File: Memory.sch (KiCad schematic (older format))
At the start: 16 parts, among them U10 74LS05, U11 74HCT00, U12 74LS32, U2 AS6C4008-55PCN, U3 AS6C4008-55PCN, U4 AS6C4008-55PCN, U5 AS6C4008-55PCN, U6 74HCT00, U7 74LS32, U8 74LS32, U9 74LS05

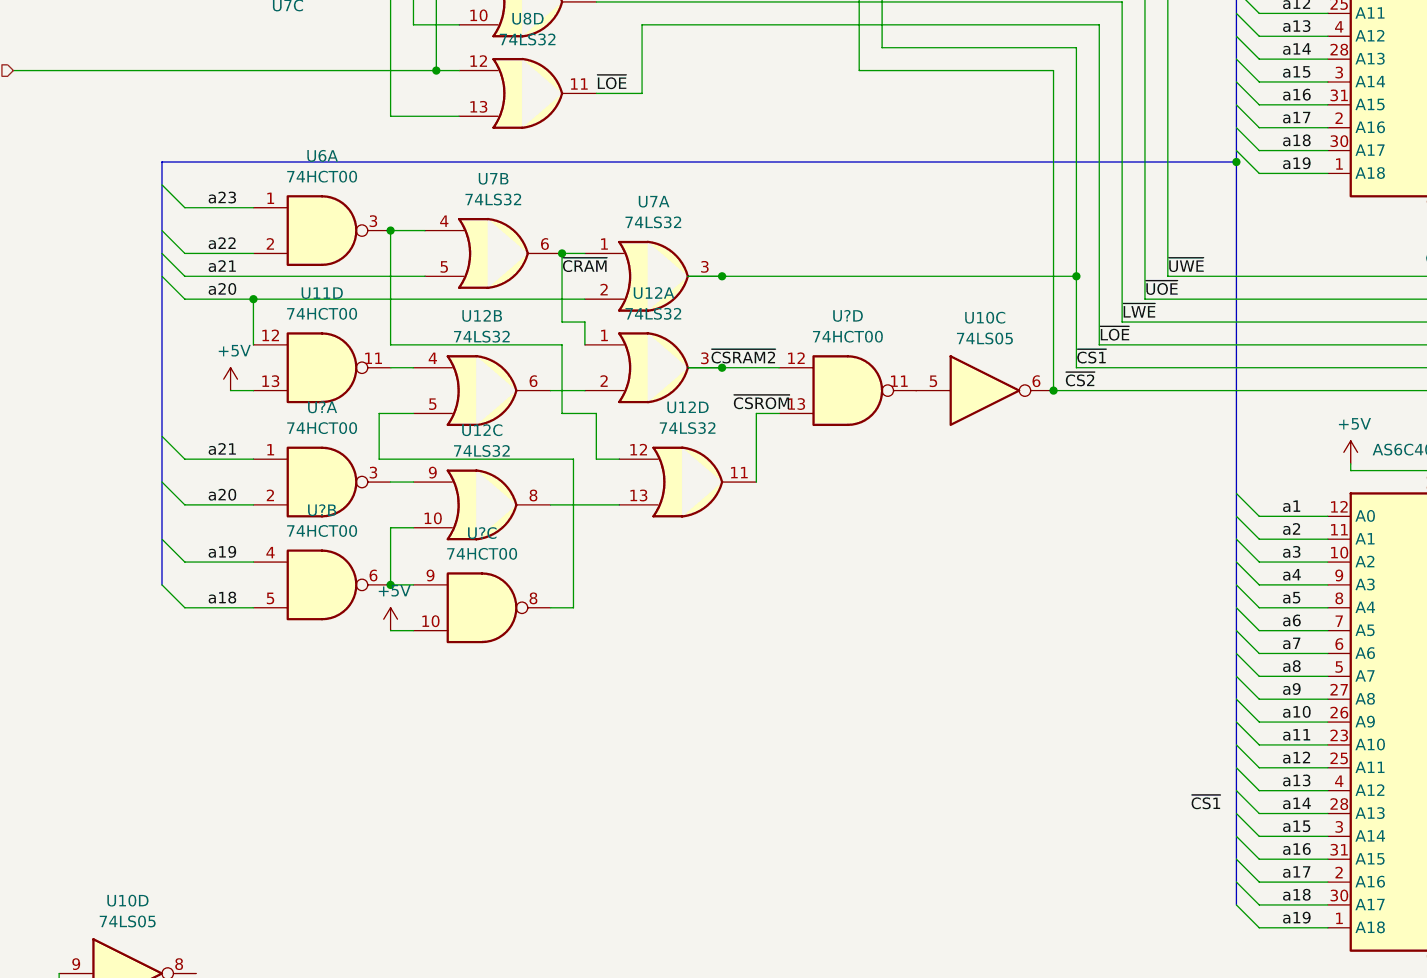
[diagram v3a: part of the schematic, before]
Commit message: jumper for rom size
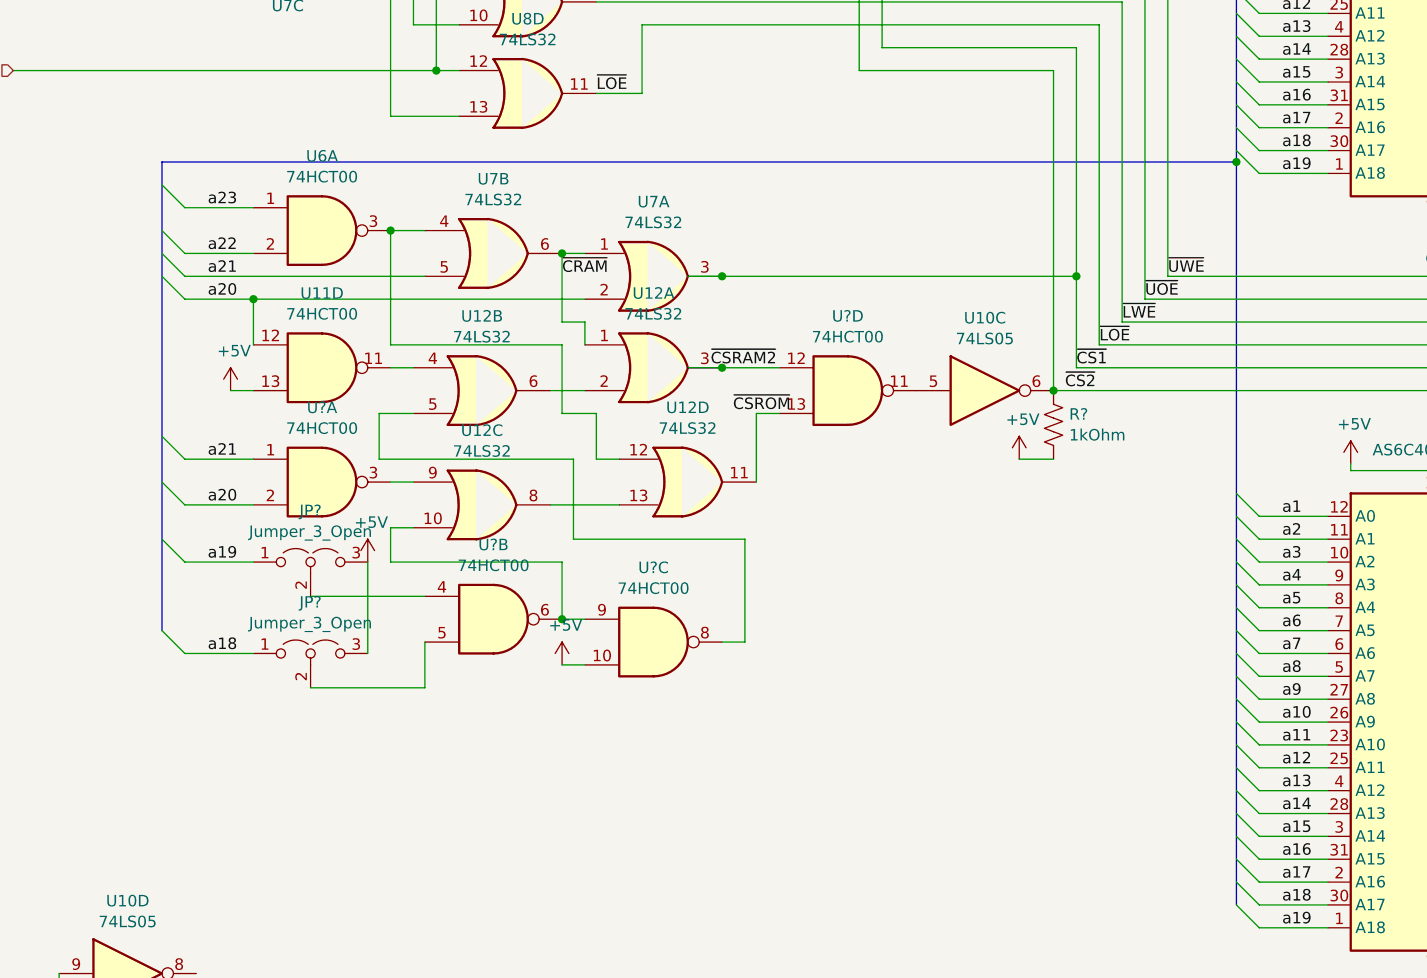
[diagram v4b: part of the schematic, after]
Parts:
- added JP? (x2): Jumper_3_Open, symbol jumper:Jumper_3_Open
- added R?: 1kOhm, symbol device:R_US
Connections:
- net +5V: now also JP?.3 (B), JP?.3 (B), R?.2
- net a18: now also JP?.1 (A); no longer U?.5
- net a19: now also JP?.1 (A); no longer U?.4
- net ~CS2: now also R?.1
- new net: JP?.2 (C), U?.5
- new net: JP?.2 (C), U?.4
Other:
- moved on the sheet: U?B, U?C

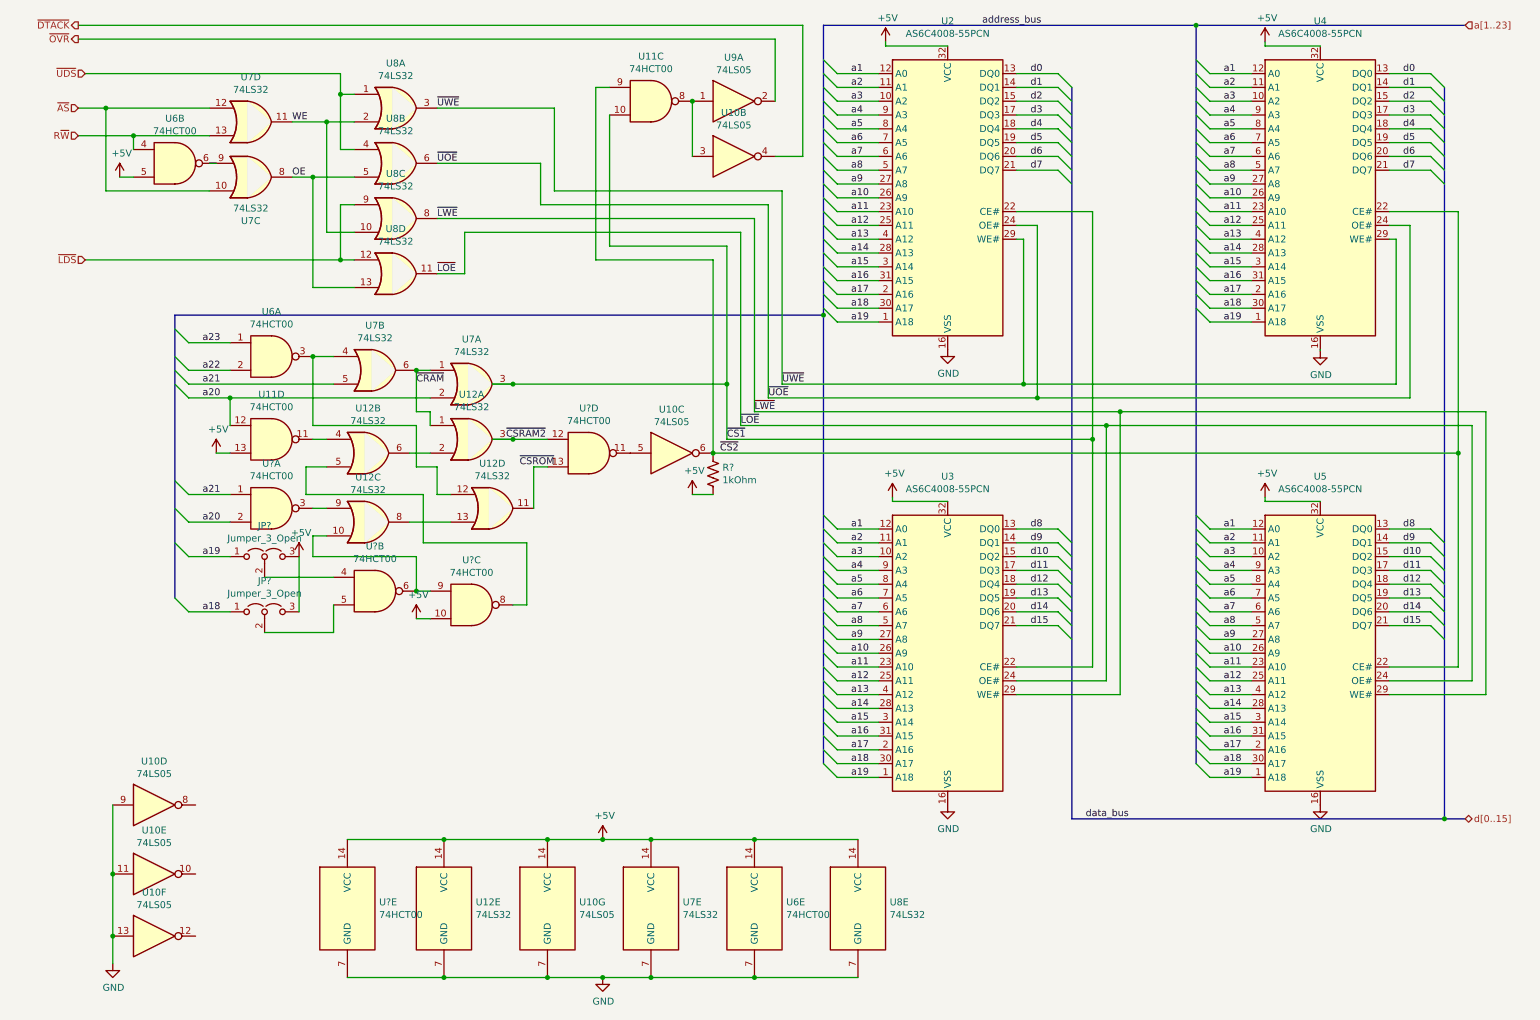
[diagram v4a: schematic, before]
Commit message: add battery
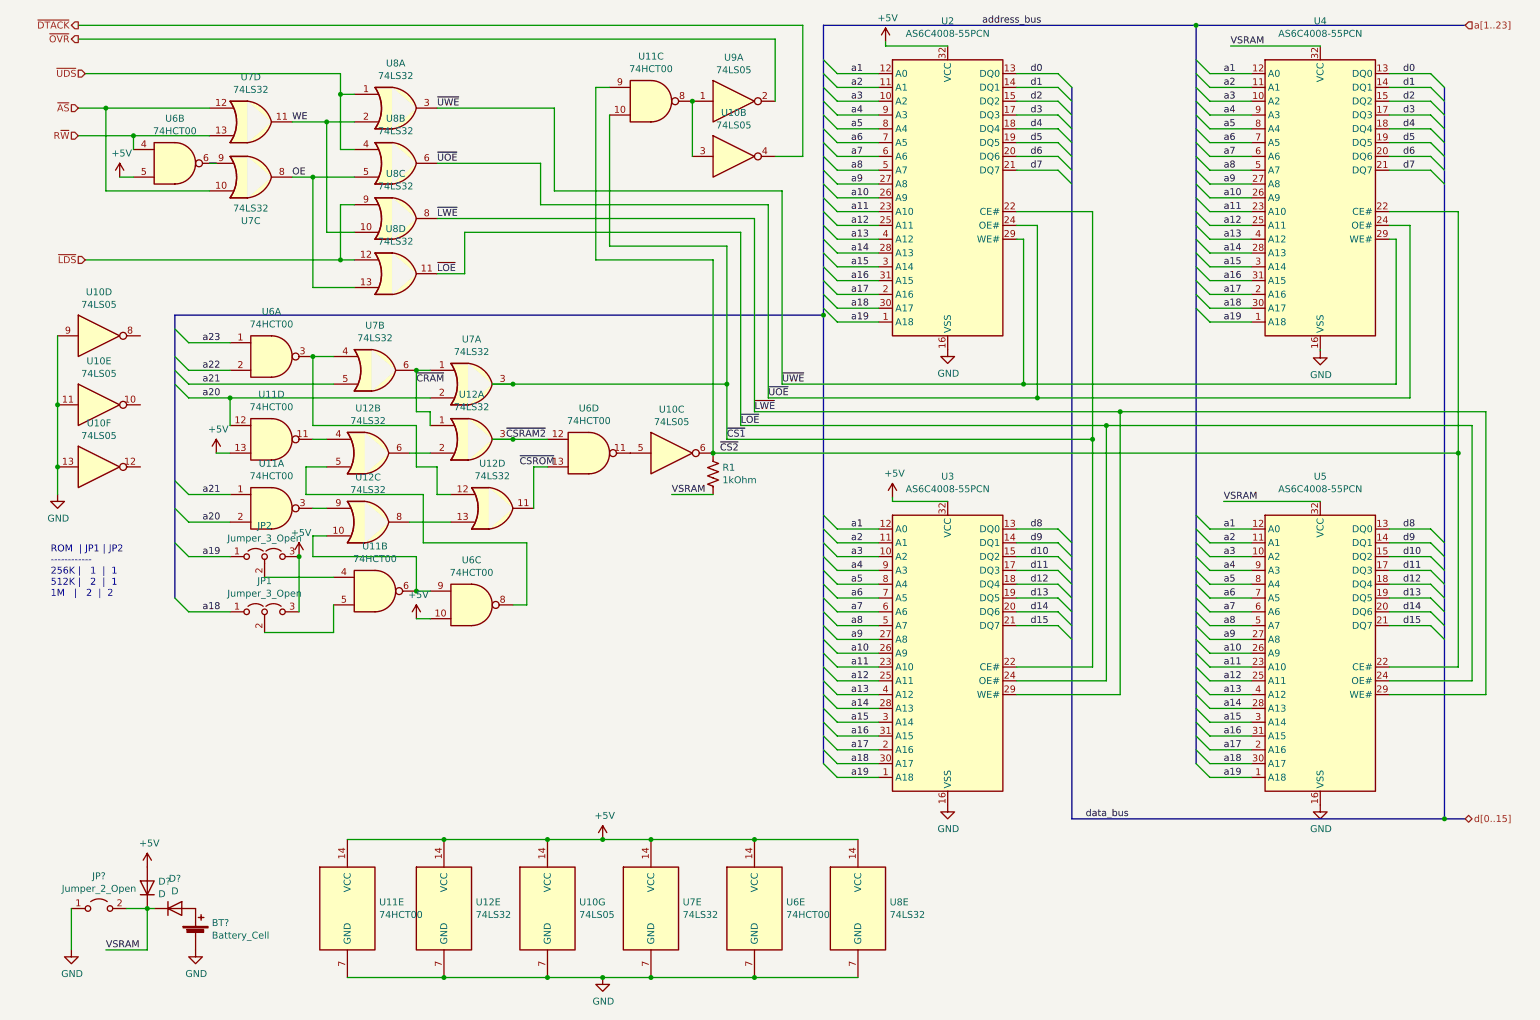
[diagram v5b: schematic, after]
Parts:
- added BT?: Battery_Cell, symbol device:Battery_Cell
- added D? (x2): D, symbol device:D
- added JP?: Jumper_2_Open, symbol jumper:Jumper_2_Open
- gave numbers to parts that had none: 5
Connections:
- net +5V: now also D?.2 (A); no longer R1.2, U4.32 (VCC), U5.32 (VCC)
- net GND: now also BT?.2 (-), JP?.1 (A)
- net a18: now also JP1.1 (A); no longer JP2.1 (A)
- net a19: now also JP2.1 (A); no longer JP1.1 (A)
- net at JP2.2 (C): now also U11.4; no longer U11.5
- net at JP1.2 (C): now also U11.5; no longer U11.4
- new net: BT?.1 (+), D?.2 (A)
- new net VSRAM: D?.1 (K), D?.1 (K), JP?.2 (B), R1.2, U4.32 (VCC), U5.32 (VCC)
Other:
- note added: "ROM | JP1 | JP2\n------------\n256K | 1 | 1\n512K | 2 | 1\n1M | 2 | 2"
- moved on the sheet: JP1, JP2, U10D, U10E, U10F

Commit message: simplyfy
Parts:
- R1: value 1kOhm -> 500Ohm
- gave numbers to parts that had none: 4
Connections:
- net +5V: no longer U11.13
- net GND: now also JP3.2 (B); no longer JP3.1 (A)
- net OE: now also U6.6; no longer U7.8
- net R~W: now also U8.10, U8.2; no longer U7.13
- net VSRAM: no longer JP3.2 (B)
- net ~AS: no longer U7.10, U7.12
- net ~CSROM: now also U12.11, U6.13
- net at BT1.1 (+), D2.2 (A): now also JP3.1 (A)
- net at U6.3, U7.4: now also U12.10; no longer U12.12
- net at U7.9: no longer U6.6
- net at U12.5: no longer U6.8
- removed net WE: U7.11, U8.10, U8.2
- new net: U11.13, U11.6, U12.12
- now unconnected: U6.9
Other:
- moved on the sheet: JP3, U12B, U6B, U6C, U7C, U7D

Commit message: rearange
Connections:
- net a20: now also U11.13, U7.5; no longer U11.12, U7.2
- net a21: now also U7.2; no longer U7.5
- net ~CRAM: now also U7.3, U7.4; no longer U7.1, U7.6
- net ~CS1: now also U7.6; no longer U7.3
- net ~CSRAM2: now also U6.13; no longer U6.12
- net ~CSROM: now also U6.12, U7.8; no longer U12.11, U6.13
- net at U7.10: now also U11.12, U11.6
- net at U7.9: now also U7.11
- net at U7.12: now also U6.3, U7.1
- net at U7.13: now also U11.3
- net at U12.4: no longer U11.11
- net at U12.6: no longer U12.2
- net at U12.8: no longer U12.13
- net at U12.9: no longer U11.3
- new net: U11.11, U12.2
- now unconnected: U12.10, U12.12
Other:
- moved on the sheet: JP1, JP2, U11A, U11B, U11D, U12A, U12C, U12D, U7A, U7B, U7C, U7D

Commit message: more rearange
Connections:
- net +5V: now also U11.10; no longer U6.10, U6.5
- net OE: now also U11.8; no longer U6.6
- net R~W: now also U11.9; no longer U6.4
- net a20: now also U6.10, U6.12; no longer U11.13, U11.2
- net a21: now also U6.9; no longer U11.1
- net ~CS1: now also U11.5; no longer U11.10
- net ~CS2: now also U11.4; no longer U11.9
- net ~CSRAM2: now also U11.1; no longer U6.13
- net ~CSROM: now also U11.2; no longer U6.12
- net at JP2.2 (C): now also U6.4; no longer U11.4
- net at JP1.2 (C): now also U6.5; no longer U11.5
- net at U7.11: now also U7.10; no longer U7.9
- net at U7.13: now also U6.8; no longer U11.3
- net at U10.3, U9.1: now also U11.6; no longer U11.8
- net at U10.5: now also U11.3; no longer U6.11
- net at U11.11: no longer U12.2
- new net: U6.13, U6.6, U7.9
- new net: U12.2, U6.11
- now unconnected: U11.12
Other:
- moved on the sheet: JP1, JP2, U11A, U11B, U11C, U11D, U12A, U12B, U12C, U12D, U6A, U6B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
